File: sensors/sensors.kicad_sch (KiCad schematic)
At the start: 19 parts, among them J1 GPIO, J10 DSHOT4, J11 DSHOT5, J12 DSHOT6, J13 DSHOT7, J14 DSHOT8, J2 JP_CAN, J3 JP_PWM, J4 JP_ADC, J5 JP_GPS, J6 JP_RADIO, J7 DSHOT1, J8 DSHOT2, J9 DSHOT3

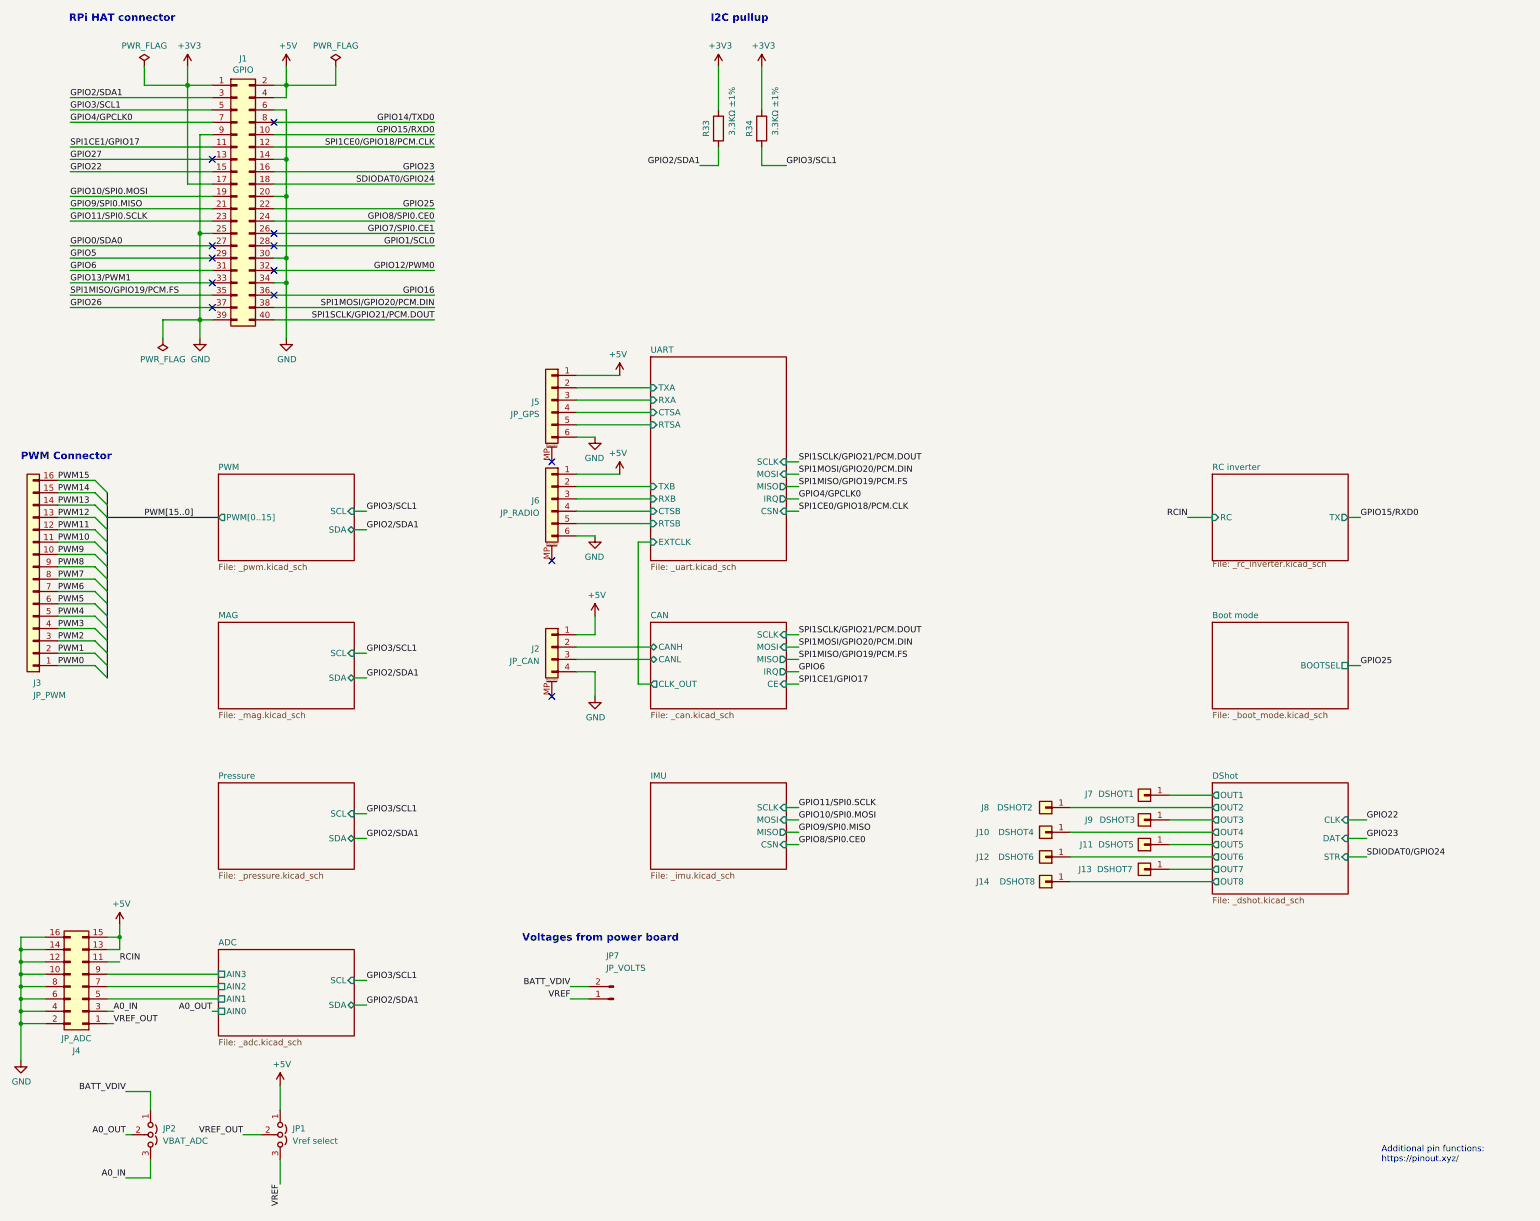
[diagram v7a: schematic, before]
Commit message: connect SIPO to SPI
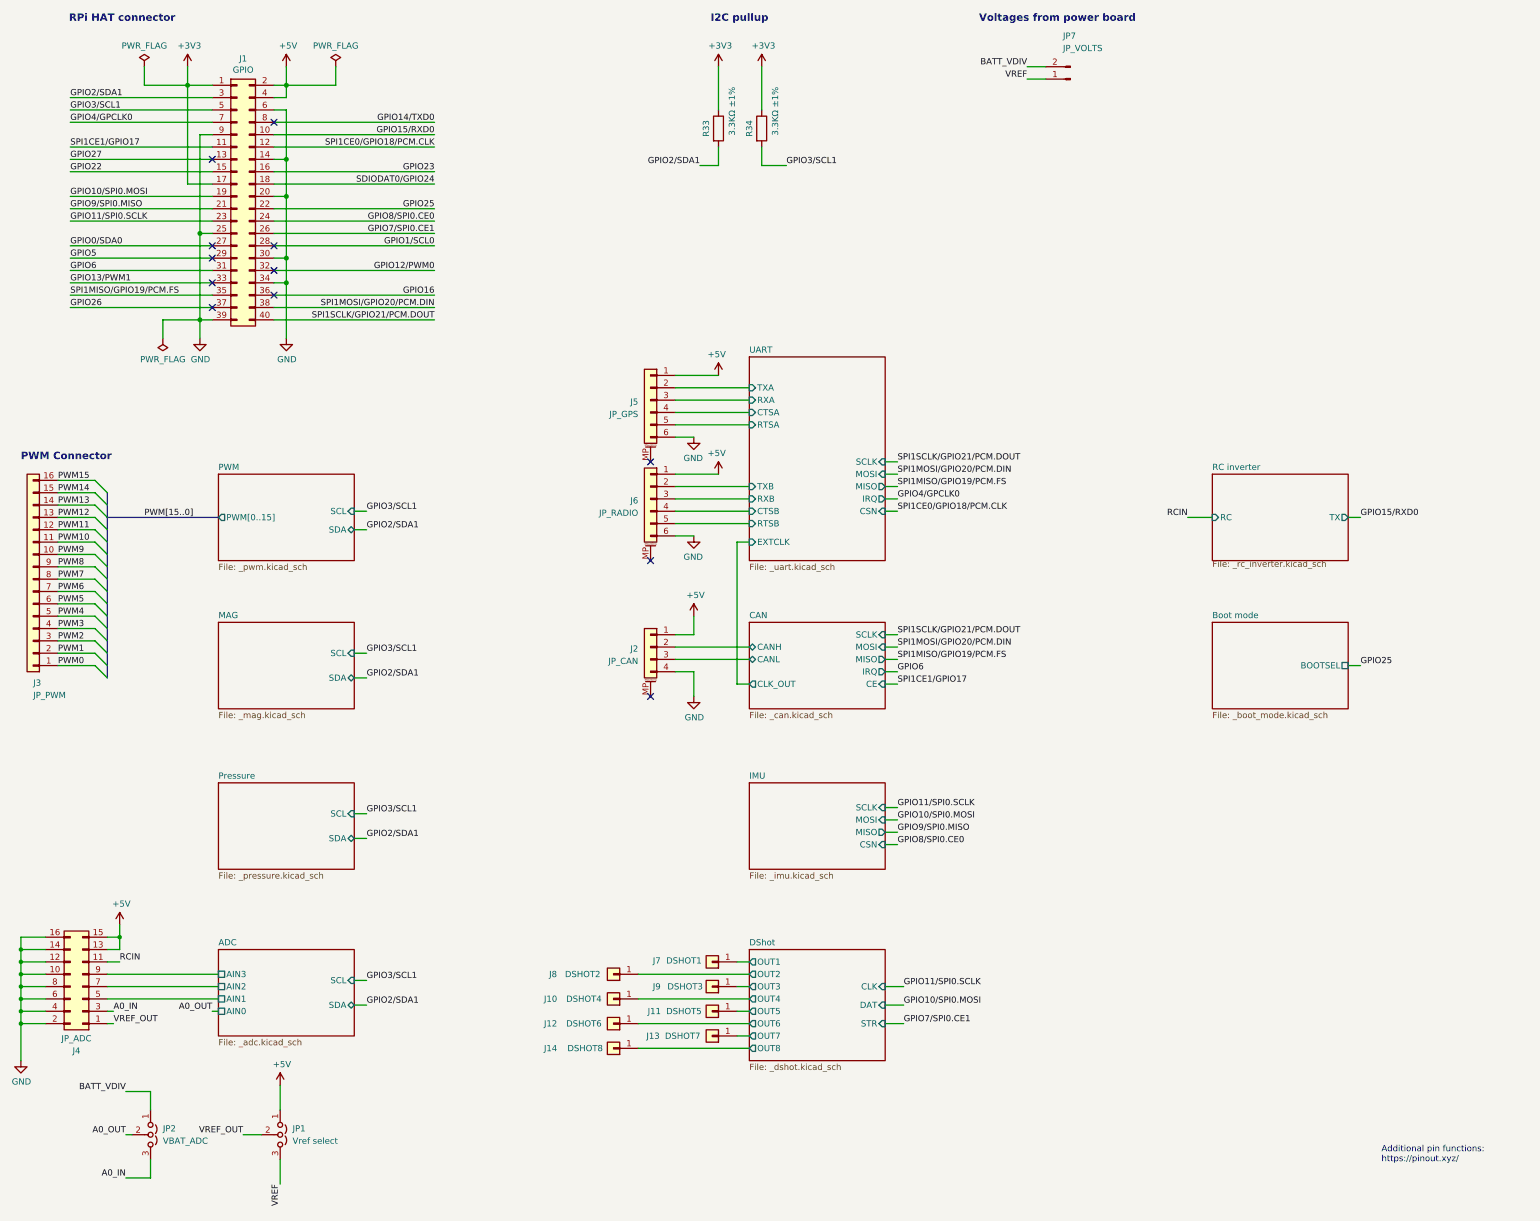
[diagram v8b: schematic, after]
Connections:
- no-connect marks 13 -> 12
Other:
- moved on the sheet: J10, J11, J12, J13, J14, J2, J5, J6, J7, J8, J9, JP7
